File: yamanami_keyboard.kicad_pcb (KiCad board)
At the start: 2 copper layers, 262.5 x 106.5 mm, 149 parts, among them J1 Breakaway_Tabs, J10 Conn_01x04, J11 Breakaway_Tabs, J12 Breakaway_Tabs, J13 Breakaway_Tabs, J14 Breakaway_Tabs, J2 Breakaway_Tabs, J3 Breakaway_Tabs, J4 Breakaway_Tabs, J5 Conn_02x03_Odd_Even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

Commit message: 配線完了
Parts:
- removed the C12 at (310.0, 142.0)
- removed the C12 at (297.3, 147.6)
- added C12: 0.1uF, Capacitor_SMD:C_0603_1608Metric, B.Cu at (306.3, 142.0)
- D50: moved to B.Cu
- moved D50 132.1 mm to (307.9, 103.1)
- moved C9 25.8 mm to (294.4, 147.6)
- moved C10 25.8 mm to (294.4, 153.9), turned to 180 degrees
- moved Y2 25.5 mm to (294.7, 150.7), turned to 0 degrees
- moved R8 20.5 mm to (316.8, 145.2), turned to 0 degrees
- moved C11 17.8 mm to (317.4, 148.4)
- moved C15 13.8 mm to (299.2, 157.9), turned to 180 degrees
- moved C18 4.32 mm to (310.3, 142.0)
- moved C13 4.32 mm to (299.2, 147.6)
- moved D45 2.78 mm to (289.7, 166.2)
- moved R12 2.43 mm to (319.0, 88.8)
- moved R9 2.43 mm to (319.0, 91.2)
- moved J1 2.00 mm to (202.7, 92.0)
- moved J11 2.00 mm to (248.7, 92.0)
- moved D44 1.87 mm to (269.6, 166.7)
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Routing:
- net GNDA: track 0.00 -> 295.3 mm, vias 0 -> 2
- net row0: track 0.00 -> 243.1 mm, vias 0 -> 2
- net row0_R: track 0.00 -> 238.8 mm, vias 0 -> 2
- net +5VA: track 0.00 -> 207.0 mm, vias 0 -> 3
- net row3_R: track 0.00 -> 159.4 mm, vias 0 -> 6
- net col5: track 0.00 -> 155.8 mm, vias 0 -> 2
- net col4: track 0.00 -> 149.6 mm, vias 0 -> 2
- net row1_R: track 0.00 -> 139.2 mm, vias 0 -> 3
- net col1_R: track 0.00 -> 135.7 mm, vias 0 -> 2
- net col0_R: track 0.00 -> 134.5 mm, vias 0 -> 2
- net col2_R: track 0.00 -> 133.9 mm, vias 0 -> 2
- net GND: track 426.9 -> 296.5 mm, vias 20 -> 2
- net row1: track 0.00 -> 128.5 mm, vias 0 -> 3
- net col2: track 0.00 -> 120.2 mm, vias 0 -> 3
- net row3: track 0.00 -> 120.1 mm, vias 0 -> 2
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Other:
- outline, holes or cut-outs redrawn
- rule trace_min: 0.2 -> 0

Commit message: fixed symbol.
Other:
- outline, holes or cut-outs redrawn

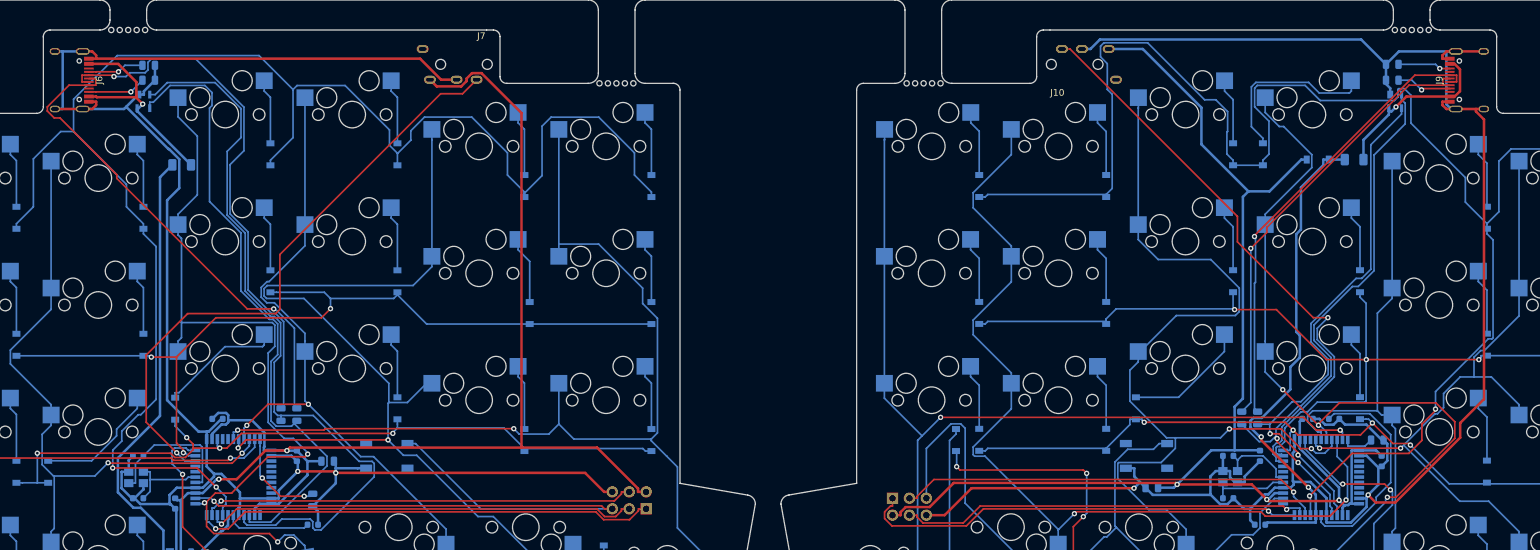
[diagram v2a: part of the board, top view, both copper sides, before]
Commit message: 配線の修正完了
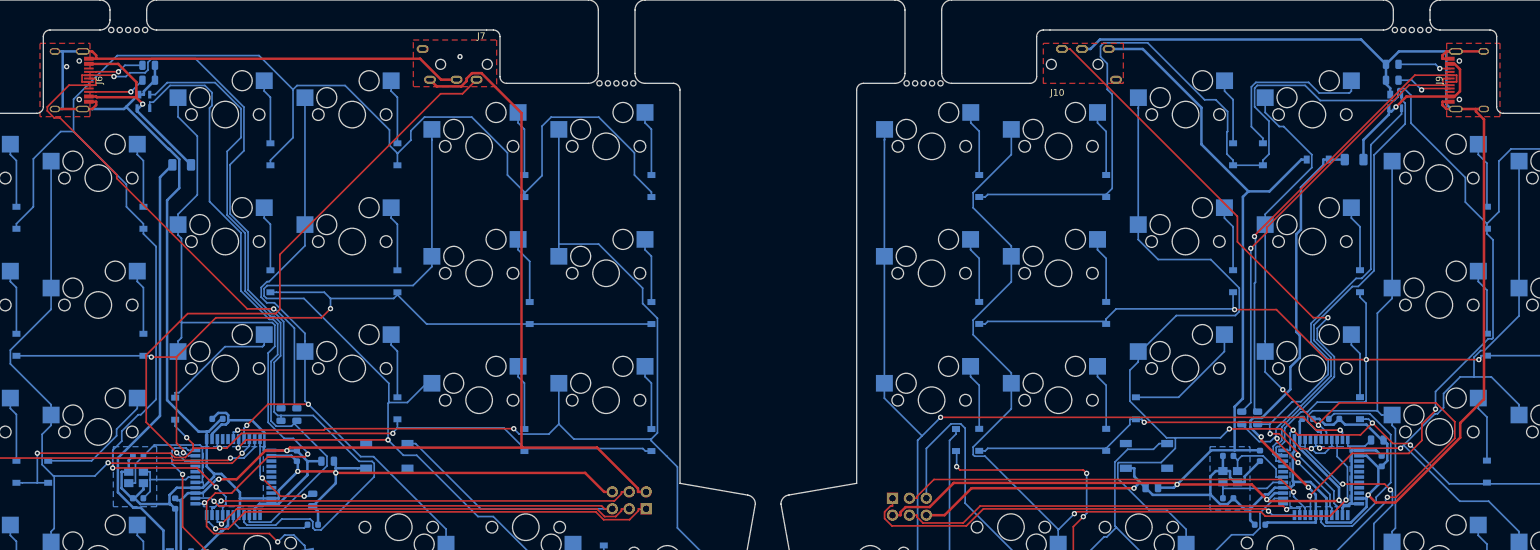
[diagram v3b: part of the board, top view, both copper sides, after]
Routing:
- net GND: vias 2 -> 4
- added copper zone on B.Cu, net GND
- added copper zone on F.Cu, net GND
- added copper zone on B.Cu, net GNDA
- added copper zone on F.Cu, net GNDA

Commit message: 大改修前の保存
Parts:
- added J15: Conn_01x01, Connector_Pin:Pin_D1.0mm_L10.0mm, F.Cu at (98.5, 152.2)
- added J16: Conn_01x01, Connector_Pin:Pin_D1.0mm_L10.0mm, F.Cu at (98.5, 148.7)
- added J19: Conn_01x01, Connector_Pin:Pin_D1.0mm_L10.0mm, F.Cu at (351.2, 148.9)
- added J20: Conn_01x01, Connector_Pin:Pin_D1.0mm_L10.0mm, F.Cu at (351.2, 152.2)
- moved D42 15.1 mm to (337.2, 149.8)
- moved C8 3.83 mm to (160.9, 158.0), turned to 90 degrees
- moved C11 3.39 mm to (319.9, 150.7)
- moved R10 2.83 mm to (296.0, 141.9)
- moved R11 2.73 mm to (299.2, 141.9)
- moved C5 2.51 mm to (134.9, 152.7)
- moved R6 2.38 mm to (154.7, 141.4)
- moved R5 2.38 mm to (152.3, 141.4)
- moved C3 1.39 mm to (143.2, 140.7), turned to 180 degrees
- moved R8 1.22 mm to (317.8, 145.9)
- moved C12 0.68 mm to (306.0, 141.4)
- moved C18 0.61 mm to (310.5, 141.4)
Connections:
- D1 pad 1: row0 -> col1
- D10 pad 1: row1 -> col1
- D11 pad 1: row1 -> col1
- D12 pad 1: row1 -> col1
- D2 pad 1: row0 -> col1
- D25 pad 1: row0_R -> col1_R
- D26 pad 1: row0_R -> col1_R
- D27 pad 1: row0_R -> col1_R
- D28 pad 1: row0_R -> col1_R
- D29 pad 1: row0_R -> col1_R
- D3 pad 1: row0 -> col1
- D30 pad 1: row0_R -> col1_R
- D31 pad 1: row1_R -> col1_R
- D32 pad 1: row1_R -> col1_R
- D33 pad 1: row1_R -> col1_R
- D34 pad 1: row1_R -> col1_R
- D35 pad 1: row1_R -> col1_R
- D36 pad 1: row1_R -> col1_R
- D4 pad 1: row0 -> col1
- D5 pad 1: row0 -> col1
- D6 pad 1: row0 -> col1
- D7 pad 1: row1 -> col1
- D8 pad 1: row1 -> col1
- D9 pad 1: row1 -> col1
- MX10 pad 1: col3 -> col1
- MX11 pad 1: col4 -> col1
- MX15 pad 1: col2 -> col1
- MX16 pad 1: col3 -> col1
- MX17 pad 1: col4 -> col1
- MX21 pad 1: col2 -> col1
- MX22 pad 1: col3 -> col1
- MX23 pad 1: col4 -> col1
- MX27 pad 1: col2_R -> col1_R
- MX28 pad 1: col3_R -> col1_R
- MX29 pad 1: col4_R -> col1_R
- MX3 pad 1: col2 -> col1
- MX33 pad 1: col2_R -> col1_R
- MX34 pad 1: col3_R -> col1_R
- MX35 pad 1: col4_R -> col1_R
- MX39 pad 1: col2_R -> col1_R
- MX4 pad 1: col3 -> col1
- MX40 pad 1: col3_R -> col1_R
- MX41 pad 1: col4_R -> col1_R
- MX45 pad 1: col2_R -> col1_R
- MX46 pad 1: col3_R -> col1_R
- MX47 pad 1: col4_R -> col1_R
- MX5 pad 1: col4 -> col1
- MX9 pad 1: col2 -> col1
- R1 pad 2: GND -> RESET
- R10 pad 1: D-_R -> D+_R
- R11 pad 1: D+_R -> D-_R
- R5 pad 1: D- -> D+
- R6 pad 1: D+ -> D-
- R7 pad 2: GNDA -> RESET_R
- U1 pad 12: col2 -> col1
- U1 pad 18: Net-(U1-Pad18) -> reserve1
- U1 pad 19: Net-(U1-Pad19) -> reserve2
- U1 pad 21: row1 -> col1
- U1 pad 29: col4 -> col1
- U1 pad 30: col3 -> col1
- U1 pad 8: row0 -> col1
- U2 pad 2: D+ -> Net-(J6-Pad6)
- U2 pad 3: D- -> Net-(J6-Pad5)
- U3 pad 18: Net-(U3-Pad18) -> reserve1_R
- U3 pad 19: Net-(U3-Pad19) -> reserve2_R
- U3 pad 21: row1_R -> col1_R
- U3 pad 28: col4_R -> col1_R
- U3 pad 29: col3_R -> col1_R
- U3 pad 30: col2_R -> col1_R
- U3 pad 8: row0_R -> col1_R
- U4 pad 2: D+_R -> Net-(J9-Pad6)
- U4 pad 3: D-_R -> Net-(J9-Pad5)
- Y1 pad 1: GND -> XTAL2
- Y1 pad 2: XTAL1 -> GND
- Y1 pad 3: GND -> XTAL1
- Y1 pad 4: XTAL2 -> GND
- Y2 pad 1: GNDA -> XTAL1_R
- Y2 pad 2: XTAL1_R -> GNDA
- Y2 pad 3: GNDA -> XTAL2_R
- Y2 pad 4: XTAL2_R -> GNDA
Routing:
- net GND: track 296.5 -> 0.00 mm, vias 4 -> 0
- net GNDA: track 295.3 -> 0.00 mm, vias 2 -> 0
- net row0: track 243.1 -> 0.00 mm, vias 2 -> 0
- net row0_R: track 238.8 -> 0.00 mm, vias 2 -> 0
- net +5VA: track 207.0 -> 0.00 mm, vias 3 -> 0
- net +5V: track 195.7 -> 0.00 mm, vias 2 -> 0
- net row3_R: track 159.4 -> 0.00 mm, vias 6 -> 0
- net col5: track 155.8 -> 0.00 mm, vias 2 -> 0
- net col4: track 149.6 -> 0.00 mm, vias 2 -> 0
- net row1_R: track 139.2 -> 0.00 mm, vias 3 -> 0
- net col1_R: track 135.7 -> 0.00 mm, vias 2 -> 0
- net col0_R: track 134.5 -> 0.00 mm, vias 2 -> 0
- net col2_R: track 133.9 -> 0.00 mm, vias 2 -> 0
- net row1: track 128.5 -> 0.00 mm, vias 3 -> 0
- net col2: track 120.2 -> 0.00 mm, vias 3 -> 0
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- removed copper zone on B.Cu, net GND
- removed copper zone on F.Cu, net GND
- removed copper zone on B.Cu, net GNDA
- removed copper zone on F.Cu, net GNDA

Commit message: 左手の配線ほぼ完了
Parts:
- removed J15, J16, J19, J20: Conn_01x01, Connector_Pin:Pin_D1.0mm_L10.0mm
- J10, J6, J7, J9: moved to B.Cu
- R1, R10, R11, R12, R2, R3, R4, R5, R6, R7, R8, R9: footprint Resistor_SMD:R_0805_2012Metric -> Resistor_SMD:R_0603_1608Metric
- moved J5 74.4 mm to (174.6, 88.6), turned to 270 degrees
- moved J8 70.7 mm to (271.1, 88.6)
- moved J10 64.4 mm to (239.7, 147.5)
- moved J7 64.2 mm to (211.1, 147.5)
- moved R10 61.0 mm to (327.7, 89.8), turned to 270 degrees
- moved R11 60.2 mm to (329.3, 89.8), turned to 270 degrees
- moved R6 59.7 mm to (124.0, 90.2), turned to 270 degrees
- moved R5 59.3 mm to (122.4, 90.2), turned to 270 degrees
- moved D49 57.7 mm to (104.7, 114.8)
- moved D50 42.1 mm to (348.4, 114.8), turned to 90 degrees
- moved F2 39.7 mm to (352.1, 111.8), turned to 90 degrees
- moved F1 37.1 mm to (101.2, 111.8), turned to 90 degrees
- moved C1 30.5 mm to (156.9, 137.9), turned to 180 degrees
- moved Y1 28.3 mm to (156.9, 140.5), turned to 180 degrees
- moved C2 26.3 mm to (156.9, 143.2)
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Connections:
- D1 pad 1: col1 -> row0
- D10 pad 1: col1 -> row1
- D11 pad 1: col1 -> row1
- D12 pad 1: col1 -> row1
- D2 pad 1: col1 -> row0
- D25 pad 1: col1_R -> row0_R
- D26 pad 1: col1_R -> row0_R
- D27 pad 1: col1_R -> row0_R
- D28 pad 1: col1_R -> row0_R
- D29 pad 1: col1_R -> row0_R
- D3 pad 1: col1 -> row0
- D30 pad 1: col1_R -> row0_R
- D31 pad 1: col1_R -> row1_R
- D32 pad 1: col1_R -> row1_R
- D33 pad 1: col1_R -> row1_R
- D34 pad 1: col1_R -> row1_R
- D35 pad 1: col1_R -> row1_R
- D36 pad 1: col1_R -> row1_R
- D4 pad 1: col1 -> row0
- D5 pad 1: col1 -> row0
- D6 pad 1: col1 -> row0
- D7 pad 1: col1 -> row1
- D8 pad 1: col1 -> row1
- D9 pad 1: col1 -> row1
- MX10 pad 1: col1 -> col3
- MX11 pad 1: col1 -> col4
- MX15 pad 1: col1 -> col2
- MX16 pad 1: col1 -> col3
- MX17 pad 1: col1 -> col4
- MX21 pad 1: col1 -> col2
- MX22 pad 1: col1 -> col3
- MX23 pad 1: col1 -> col4
- MX27 pad 1: col1_R -> col2_R
- MX28 pad 1: col1_R -> col3_R
- MX29 pad 1: col1_R -> col4_R
- MX3 pad 1: col1 -> col2
- MX33 pad 1: col1_R -> col2_R
- MX34 pad 1: col1_R -> col3_R
- MX35 pad 1: col1_R -> col4_R
- MX39 pad 1: col1_R -> col2_R
- MX4 pad 1: col1 -> col3
- MX40 pad 1: col1_R -> col3_R
- MX41 pad 1: col1_R -> col4_R
- MX45 pad 1: col1_R -> col2_R
- MX46 pad 1: col1_R -> col3_R
- MX47 pad 1: col1_R -> col4_R
- MX5 pad 1: col1 -> col4
- MX9 pad 1: col1 -> col2
- U1 pad 12: col1 -> col2
- U1 pad 18: reserve1 -> Net-(U1-Pad18)
- U1 pad 19: reserve2 -> Net-(U1-Pad19)
- U1 pad 21: col1 -> row1
- U1 pad 29: col1 -> col4
- U1 pad 30: col1 -> col3
- U1 pad 8: col1 -> row0
- U3 pad 18: reserve1_R -> Net-(U3-Pad18)
- U3 pad 19: reserve2_R -> Net-(U3-Pad19)
- U3 pad 21: col1_R -> row1_R
- U3 pad 28: col1_R -> col4_R
- U3 pad 29: col1_R -> col3_R
- U3 pad 30: col1_R -> col2_R
- U3 pad 8: col1_R -> row0_R
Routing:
- net GND: track 0.00 -> 386.1 mm, vias 0 -> 10
- net +5V: track 0.00 -> 216.9 mm, vias 0 -> 11
- net VBUS: track 0.00 -> 147.8 mm
- net row1: track 0.00 -> 141.0 mm, vias 0 -> 15
- net col5: track 0.00 -> 138.9 mm, vias 0 -> 15
- net row0: track 0.00 -> 138.1 mm, vias 0 -> 13
- net row3: track 0.00 -> 127.8 mm, vias 0 -> 11
- net col0: track 0.00 -> 126.9 mm, vias 0 -> 10
- net col4: track 0.00 -> 118.6 mm, vias 0 -> 16
- net row2: track 0.00 -> 114.1 mm, vias 0 -> 7
- net col1: track 0.00 -> 112.2 mm, vias 0 -> 16
- net col3: track 0.00 -> 102.8 mm, vias 0 -> 16
- net Net-(J9-Pad6): track 90.4 -> 0.00 mm, vias 3 -> 0
- net col2: track 0.00 -> 89.3 mm, vias 0 -> 13
- net Net-(J9-Pad5): track 88.6 -> 0.00 mm, vias 3 -> 0
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- added copper zone on B.Cu, net GND
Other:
- outline, holes or cut-outs redrawn
